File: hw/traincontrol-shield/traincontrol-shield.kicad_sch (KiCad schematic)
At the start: 3 parts, among them J4 Track Input, J5 Motor Windings, J6 Motor+AC

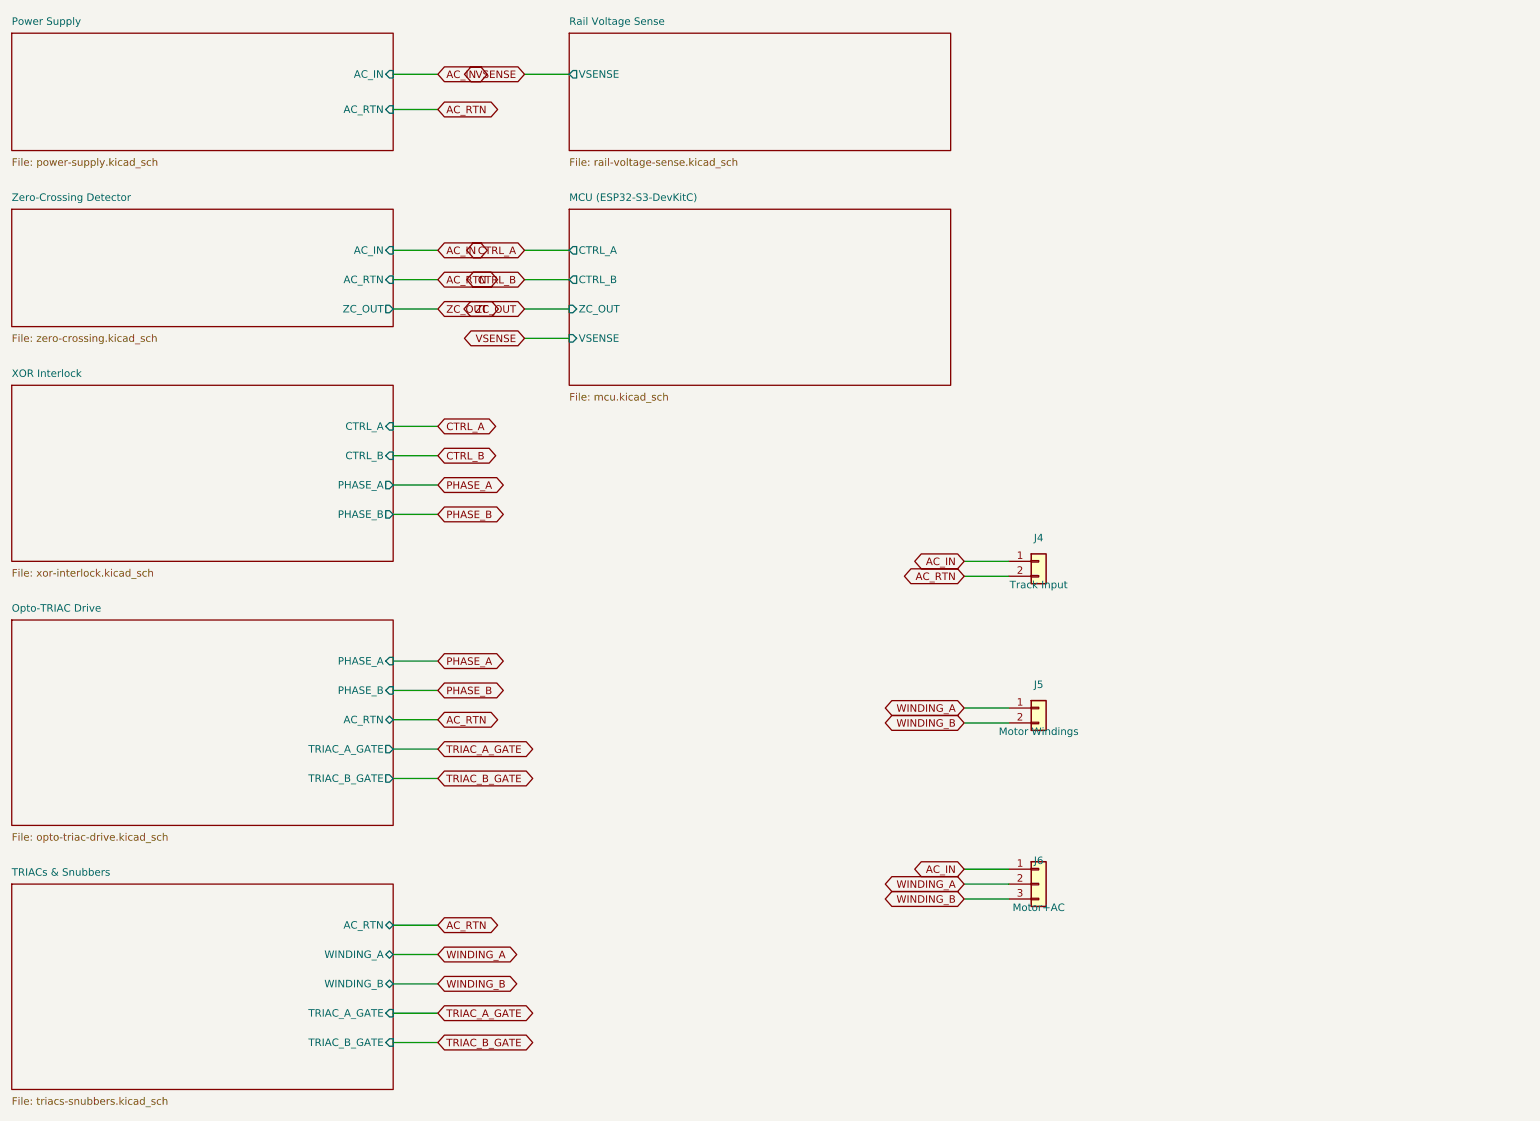
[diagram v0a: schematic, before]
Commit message: Schematic updates by hand.
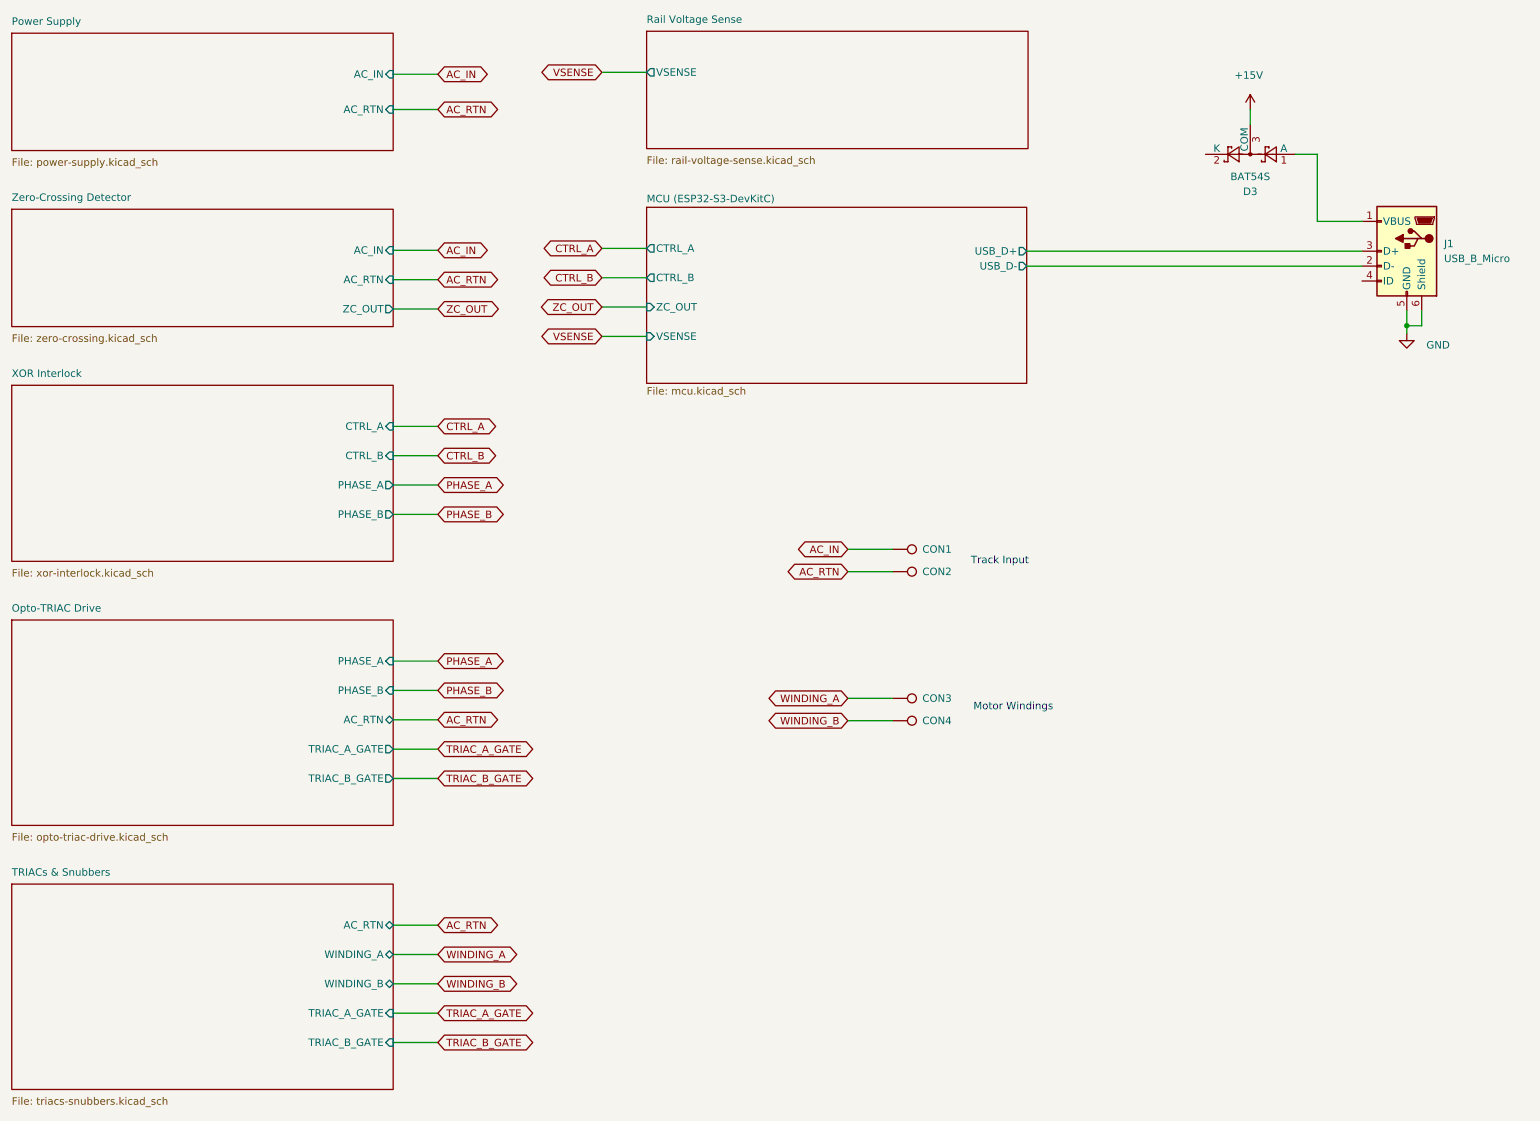
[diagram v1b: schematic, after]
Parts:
- removed J4: Track Input, TerminalBlock_Phoenix:TerminalBlock_Phoenix_MKDS-1,5-2-5.08_1x02_P5.08mm_Horizontal, symbol Connector_Generic:Conn_01x02
- removed J5: Motor Windings, TerminalBlock_Phoenix:TerminalBlock_Phoenix_MKDS-1,5-2-5.08_1x02_P5.08mm_Horizontal, symbol Connector_Generic:Conn_01x02
- removed J6: Motor+AC, TerminalBlock_Phoenix:TerminalBlock_Phoenix_MKDS-1,5-3-5.08_1x03_P5.08mm_Horizontal, symbol Connector_Generic:Conn_01x03
- added CON1, CON2, CON3, CON4: ConnectionPad, TestPoint:TestPoint_Pad_D2.0mm, symbol Connector:TestPoint
- added D3: BAT54S, Package_TO_SOT_SMD:SOT-23, symbol Diode:BAT54S
- added J1: USB_B_Micro, Connector_USB:USB_Micro-B_Molex-105017-0001, symbol Connector:USB_B_Micro
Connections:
- net AC_IN: now also CON1.1
- net AC_RTN: now also CON2.1
- net WINDING_A: now also CON3.1
- net WINDING_B: now also CON4.1
- new net: D3.1 (A), J1.1 (VBUS)
- new net +15V: D3.3 (COM)
- new net GND: J1.5 (GND), J1.6 (Shield)
- new net MCU (ESP32-S3-DevKitC)/USB_D+: J1.3 (D+)
- new net MCU (ESP32-S3-DevKitC)/USB_D-: J1.2 (D-)
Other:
- sheet MCU (ESP32-S3-DevKitC) ports: added USB_D+, USB_D-; removed none
- note added: "Motor Windings"
- note added: "Track Input"
